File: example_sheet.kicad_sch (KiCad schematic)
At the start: 5 parts, among them J1 Conn_Coaxial, J2 Conn_Coaxial

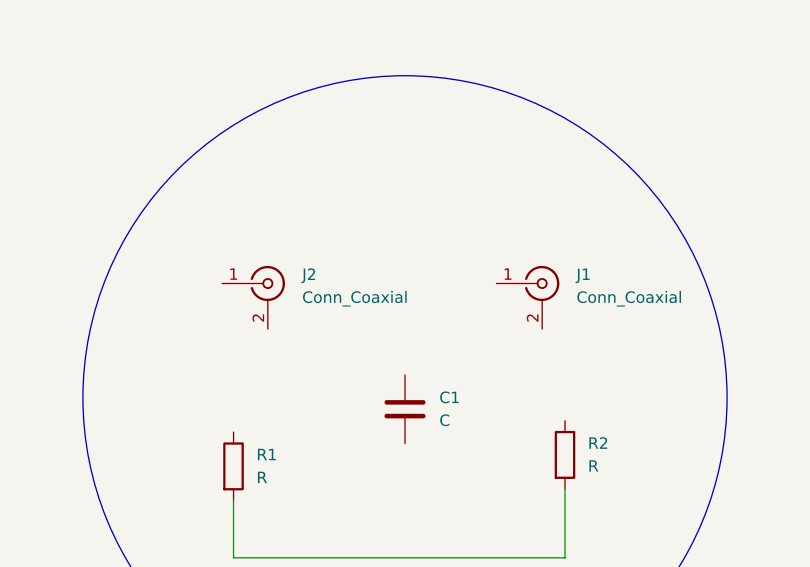
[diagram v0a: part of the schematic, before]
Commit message: new branch text added
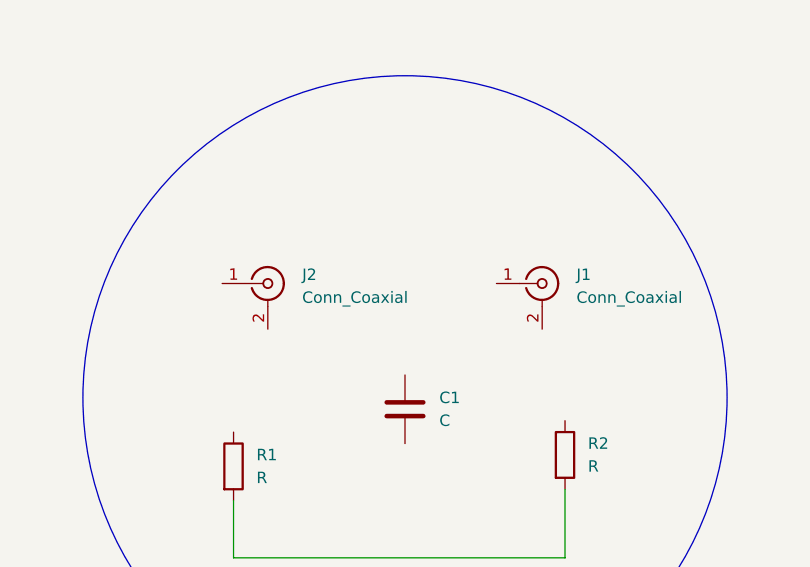
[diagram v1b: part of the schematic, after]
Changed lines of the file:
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@@
 (kicad_sch
-	(version 20231120)
+	(version 20250114)
 	(generator "eeschema")
-	(generator_version "8.0")
+	(generator_version "9.0")
 	(paper "A4")
+	(circle
+		(center 146.05 82.55)
+		(radius 35.7861)
+		(stroke
+			(width 0)
+			(type default)
+		)
+		(fill
+			(type none)
+		)
+	)
+	(text "This is an example sheet. Add whatever you want!"
+		(exclude_from_sim no)
+		(at 146.05 23.622 0)
+		(effects
+			(font
+				(size 5.08 5.08)
+				(thickness 1.016)
+				(bold yes)
+			)
+		)
+	)
 	(wire
 		(pts
@@
 		)
 	)
-	(circle
-		(center 146.05 82.55)
-		(radius 35.7861)
-		(stroke
-			(width 0)
-			(type default)
-		)
-		(fill
-			(type none)
-		)
-	)
-	(text "This is an example sheet. Add whatever you want!"
-		(exclude_from_sim no)
-		(at 146.05 23.622 0)
-		(effects
-			(font
-				(size 5.08 5.08)
-				(thickness 1.016)
-				(bold yes)
-			)
-		)
-	)
